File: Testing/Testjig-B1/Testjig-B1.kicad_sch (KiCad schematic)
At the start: 2 parts, among them J2 Conn_02x16_Odd_Even, X2 5102159-8

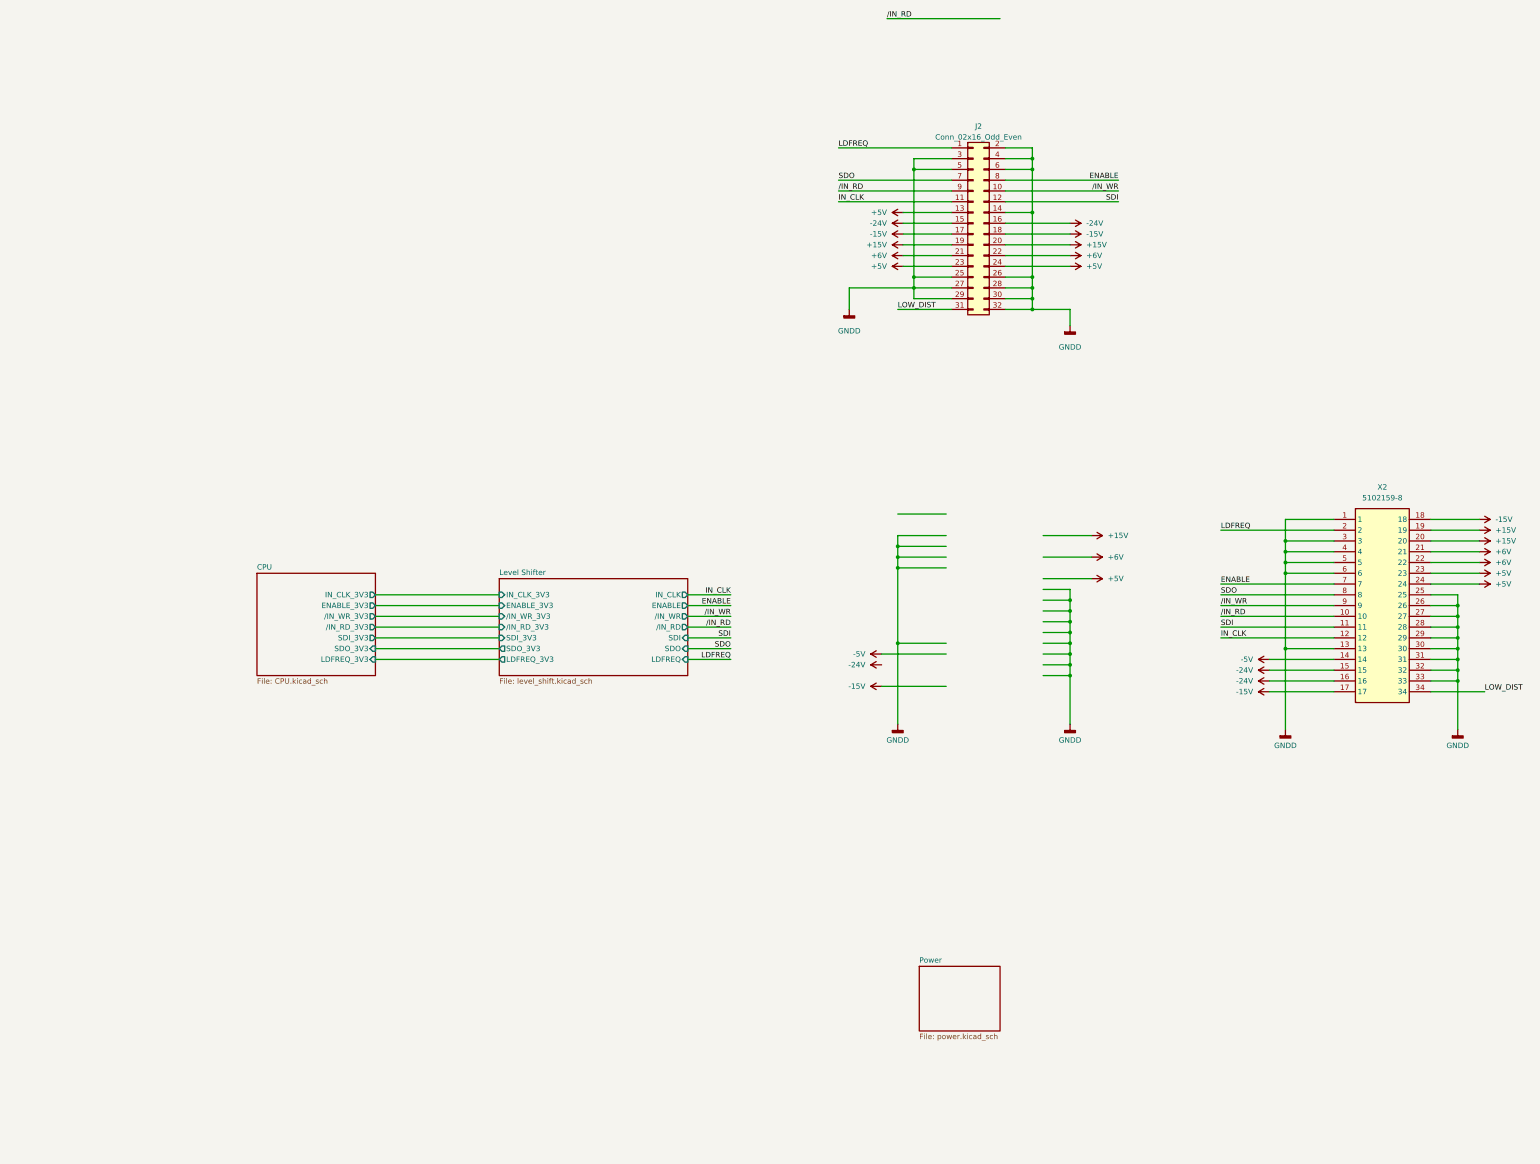
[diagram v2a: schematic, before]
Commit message: First iteration tester design
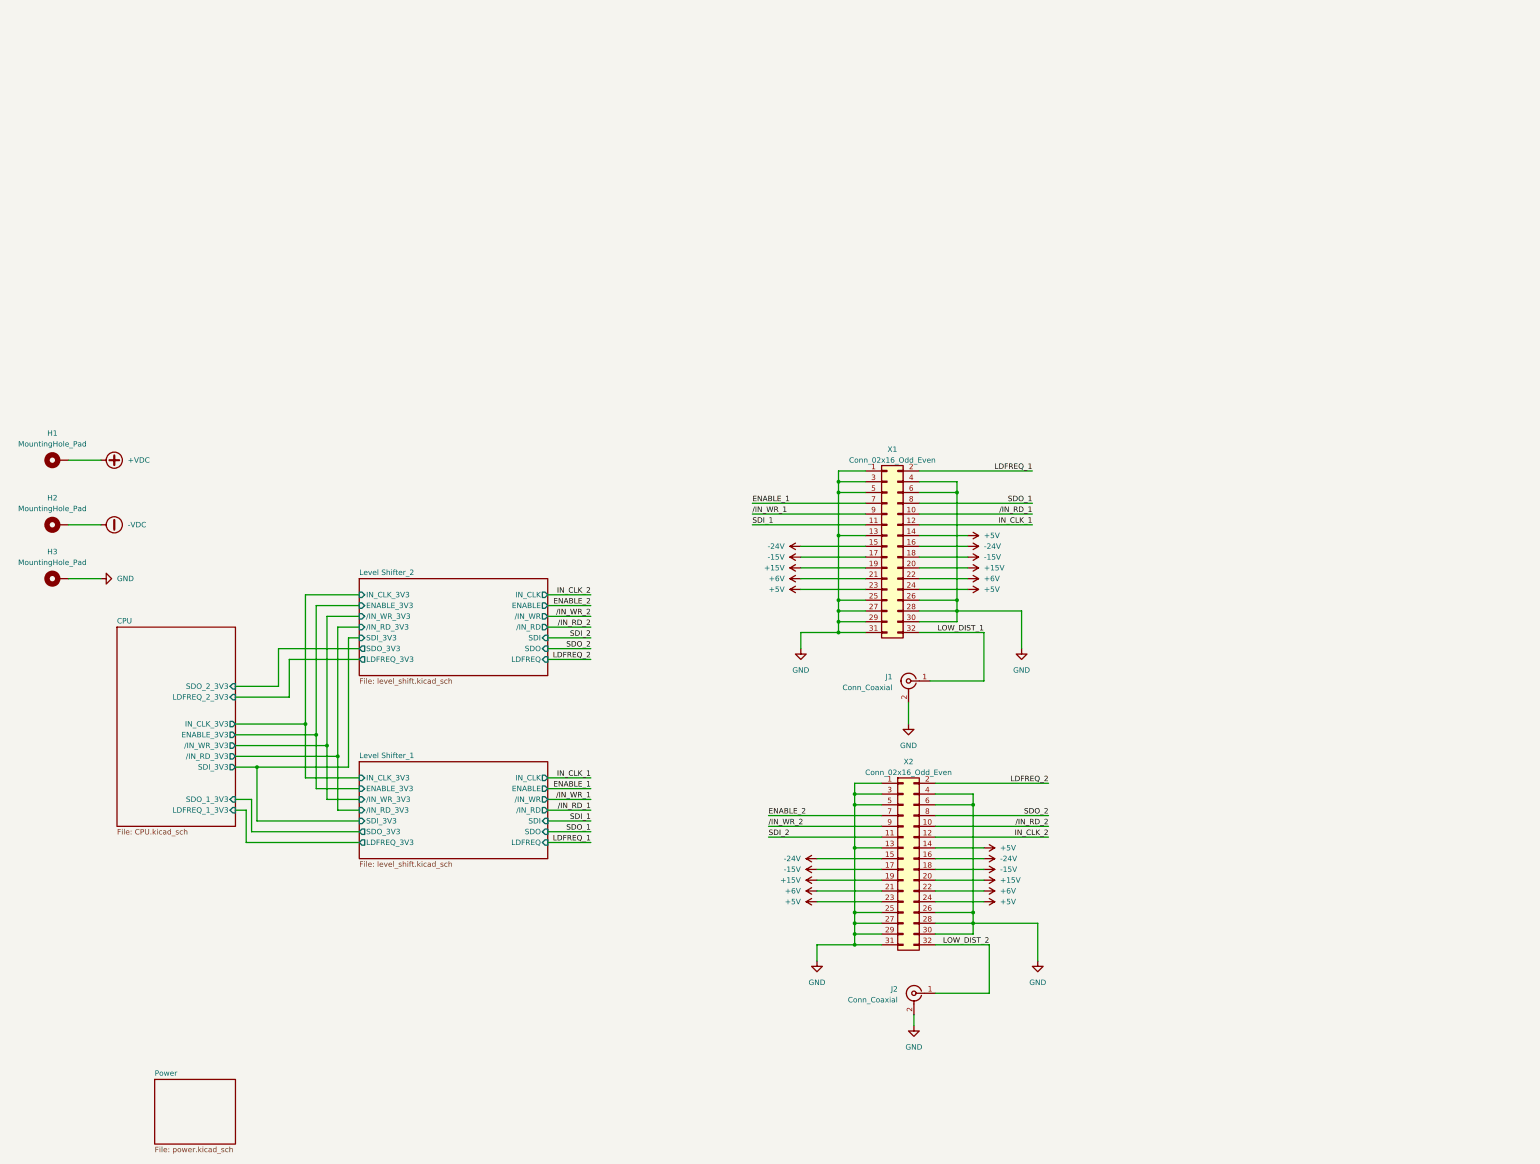
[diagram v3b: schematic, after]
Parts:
- removed X2: 5102159-8, UPL_B1:CONN_5103311-7_TYC, symbol UPL_B1:5102159-8
- added H1, H2, H3: MountingHole_Pad, MountingHole:MountingHole_6.4mm_M6_DIN965_Pad, symbol Mechanical:MountingHole_Pad
- added J1, J2: Conn_Coaxial, Connector_Coaxial:BNC_Amphenol_031-5539_Vertical, symbol Connector:Conn_Coaxial
- added X2: Conn_02x16_Odd_Even, Connector_PinHeader_2.54mm:PinHeader_2x16_P2.54mm_Vertical, symbol Connector_Generic:Conn_02x16_Odd_Even
- X1: renamed from J2; footprint (none) -> Connector_PinHeader_2.54mm:PinHeader_2x16_P2.54mm_Vertical
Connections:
- net LDFREQ is gone; now on net GND: X1.1 (Pin_1)
- net LOW_DIST is gone; now on net GND: X1.31 (Pin_31)
- net +15V: now also X2.19 (Pin_19), X2.20 (Pin_20)
- net +5V: now also X1.14 (Pin_14), X2.14 (Pin_14), X2.23 (Pin_23), X2.24 (Pin_24); no longer X1.13 (Pin_13)
- net +6V: now also X2.21 (Pin_21), X2.22 (Pin_22)
- net -15V: now also X2.17 (Pin_17), X2.18 (Pin_18)
- net -24V: now also X2.15 (Pin_15), X2.16 (Pin_16)
- net ENABLE renamed SDO_1
- net GNDD renamed GND
- net GND: now also X1.13 (Pin_13), H3.1, J1.2 (Ext), J2.2 (Ext), X2.1 (Pin_1), X2.13 (Pin_13), X2.25 (Pin_25), X2.26 (Pin_26), X2.27 (Pin_27), X2.28 (Pin_28), X2.29 (Pin_29), X2.3 (Pin_3), X2.30 (Pin_30), X2.31 (Pin_31), X2.4 (Pin_4), X2.5 (Pin_5), X2.6 (Pin_6); no longer X1.14 (Pin_14), X1.2 (Pin_2), X1.32 (Pin_32)
- net IN_CLK renamed SDI_1
- net SDI renamed IN_CLK_1
- net SDO renamed ENABLE_1
- net /IN_RD renamed /IN_WR_1
- net /IN_WR renamed /IN_RD_1
- new net +VDC: H1.1
- new net -VDC: H2.1
- new net ENABLE_2: X2.7 (Pin_7)
- new net IN_CLK_2: X2.12 (Pin_12)
- new net LDFREQ_1: X1.2 (Pin_2)
- new net LDFREQ_2: X2.2 (Pin_2)
- new net LOW_DIST_1: J1.1 (In), X1.32 (Pin_32)
- new net LOW_DIST_2: J2.1 (In), X2.32 (Pin_32)
- new net SDI_2: X2.11 (Pin_11)
- new net SDO_2: X2.8 (Pin_8)
- new net /IN_RD_2: X2.10 (Pin_10)
- new net /IN_WR_2: X2.9 (Pin_9)
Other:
- sheet Level Shifter renamed Level Shifter_1
- added sheet Level Shifter_2 (level_shift.kicad_sch)
- sheet CPU ports: added LDFREQ_1_3V3, LDFREQ_2_3V3, SDO_1_3V3, SDO_2_3V3; removed LDFREQ_3V3, SDO_3V3
- moved on the sheet: X1

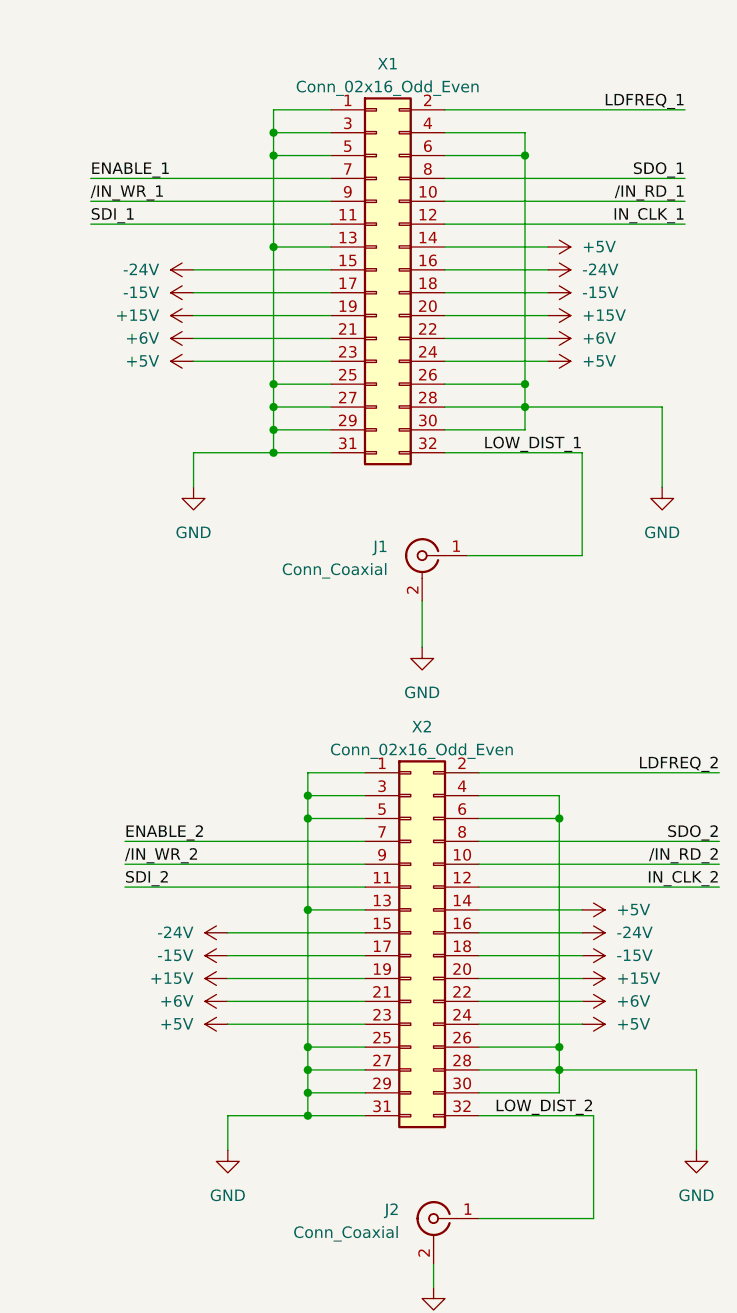
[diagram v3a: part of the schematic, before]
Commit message: Make board production ready.
- Fix all DRC errors (accept if need)
- Fix all ERC errors (accept if needed)
- Use correct 34 (!) pin connector on board
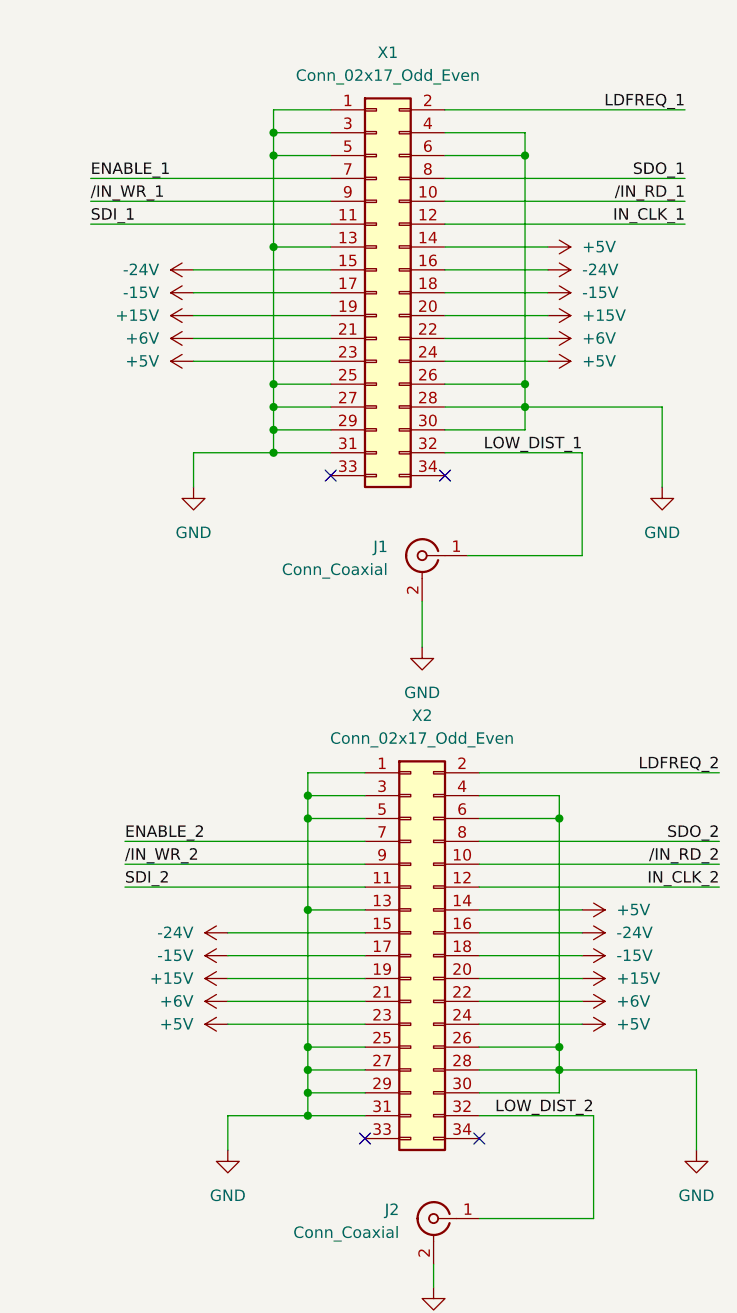
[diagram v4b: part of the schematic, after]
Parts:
- removed X1, X2: Conn_02x16_Odd_Even, Connector_PinHeader_2.54mm:PinHeader_2x16_P2.54mm_Vertical, symbol Connector_Generic:Conn_02x16_Odd_Even
- added X1, X2: Conn_02x17_Odd_Even, Connector_IDC:IDC-Header_2x17_P2.54mm_Vertical, symbol Connector_Generic:Conn_02x17_Odd_Even
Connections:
- net +15V: now also X1.19 (Pin_19), X1.20 (Pin_20), X2.19 (Pin_19), X2.20 (Pin_20)
- net +5V: now also X1.14 (Pin_14), X1.23 (Pin_23), X1.24 (Pin_24), X2.14 (Pin_14), X2.23 (Pin_23), X2.24 (Pin_24)
- net +6V: now also X1.21 (Pin_21), X1.22 (Pin_22), X2.21 (Pin_21), X2.22 (Pin_22)
- net -15V: now also X1.17 (Pin_17), X1.18 (Pin_18), X2.17 (Pin_17), X2.18 (Pin_18)
- net -24V: now also X1.15 (Pin_15), X1.16 (Pin_16), X2.15 (Pin_15), X2.16 (Pin_16)
- net ENABLE_1: now also X1.7 (Pin_7)
- net ENABLE_2: now also X2.7 (Pin_7)
- net GND: now also X1.1 (Pin_1), X1.13 (Pin_13), X1.25 (Pin_25), X1.26 (Pin_26), X1.27 (Pin_27), X1.28 (Pin_28), X1.29 (Pin_29), X1.3 (Pin_3), X1.30 (Pin_30), X1.31 (Pin_31), X1.4 (Pin_4), X1.5 (Pin_5), X1.6 (Pin_6), X2.1 (Pin_1), X2.13 (Pin_13), X2.25 (Pin_25), X2.26 (Pin_26), X2.27 (Pin_27), X2.28 (Pin_28), X2.29 (Pin_29), X2.3 (Pin_3), X2.30 (Pin_30), X2.31 (Pin_31), X2.4 (Pin_4), X2.5 (Pin_5), X2.6 (Pin_6)
- net IN_CLK_1: now also X1.12 (Pin_12)
- net IN_CLK_2: now also X2.12 (Pin_12)
- net LDFREQ_1: now also X1.2 (Pin_2)
- net LDFREQ_2: now also X2.2 (Pin_2)
- net LOW_DIST_1: now also X1.32 (Pin_32)
- net LOW_DIST_2: now also X2.32 (Pin_32)
- net SDI_1: now also X1.11 (Pin_11)
- net SDI_2: now also X2.11 (Pin_11)
- net SDO_1: now also X1.8 (Pin_8)
- net SDO_2: now also X2.8 (Pin_8)
- net /IN_RD_1: now also X1.10 (Pin_10)
- net /IN_RD_2: now also X2.10 (Pin_10)
- net /IN_WR_1: now also X1.9 (Pin_9)
- net /IN_WR_2: now also X2.9 (Pin_9)
- no-connect marks 0 -> 4
